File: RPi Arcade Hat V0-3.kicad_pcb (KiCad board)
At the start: 4 copper layers, 241.3 x 64.5 mm, 137 parts, among them J1 Raspberry_Pi_2_3, J10 Coin/Note Input, J11 +24V IN, J12 +12V OUT, J13 Player 1, J14 Player 2, J15 Player 3, J16 Player 4, J17 Counter Board, J18 HDSP-523E, J19 Coin Counter, J2 Player 1, J3 Player 2, J4 Spares, J5 Player 3, J6 Player 4, J7 +24V OUT, J8 Counter Bypass, Q1 BC847, Q10 BC847, Q11 BC847, Q12 BC847, Q13 BC847, Q14 BC847, Q15 BC847, Q16 BC847, Q2 BC847, Q3 BC847, Q4 BC847, Q5 BC847, Q6 BC847, Q7 BC847, Q8 BC847, Q9 BC847, U1 SN74HC32N, U10 NE555DR, U12 SN74HC08N, U13 NE555DR, U14 SN74HC74N, U15 SN74HC32N, U16 SN74HC32N, U18 SN74HC08N, U3 LM2595S-12, U4 4510, U6 4510, U7 4511, U8 4511, U9 NE555DR

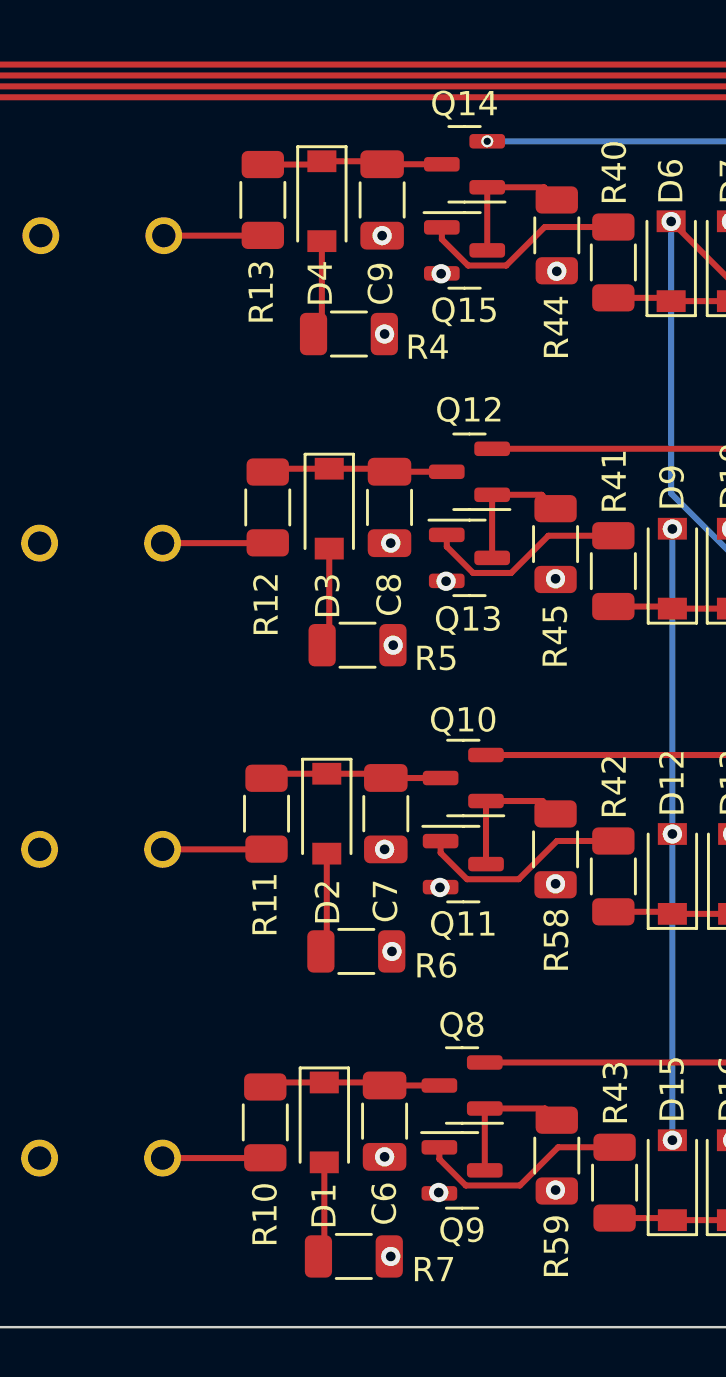
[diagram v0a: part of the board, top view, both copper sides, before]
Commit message: Found Error on Debounce Circuit
As I was going through the schematic I found I wired the button credit input incorrect, and had the logic level held high then pulling to GND, and I should've used an inverter on the output, went with a simple fix, and ended up removing the extra components and changing the connection on the button from GND to +5V
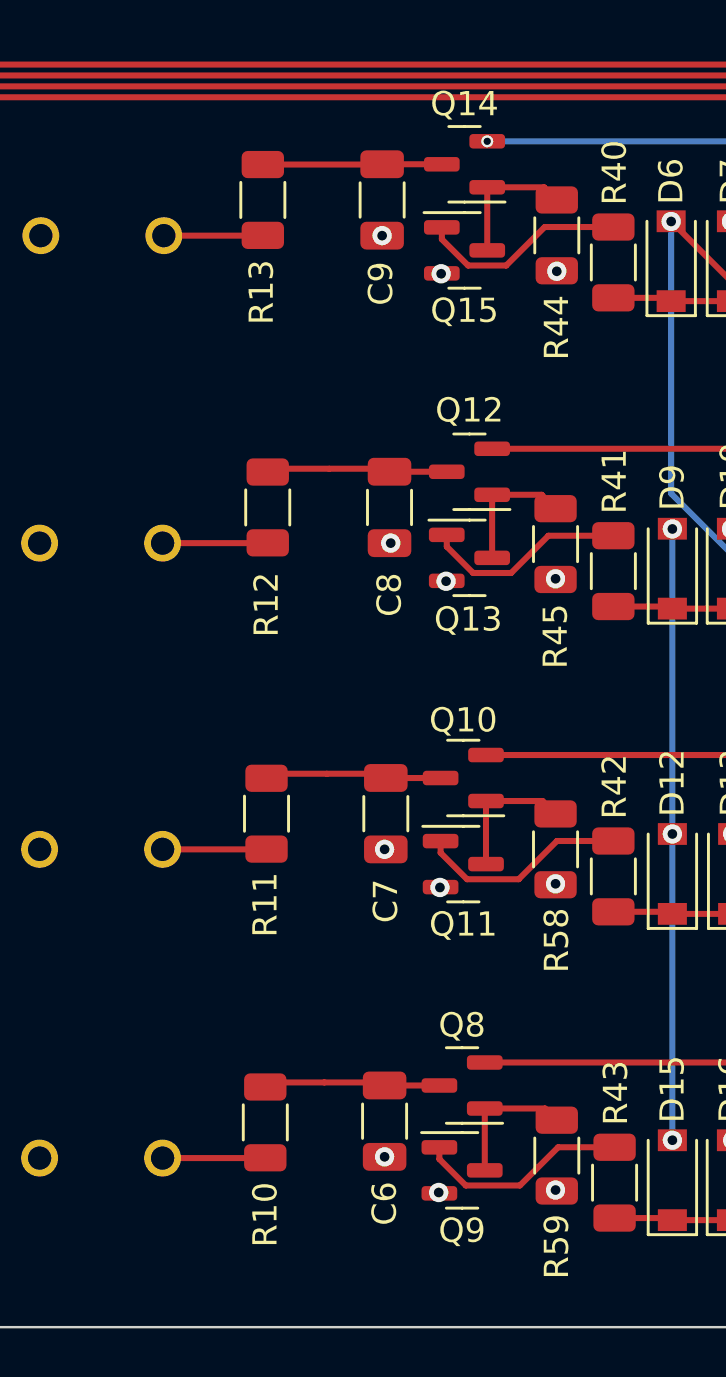
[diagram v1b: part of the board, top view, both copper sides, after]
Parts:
- removed D1, D2, D3, D4: 1N4448W, Diode_SMD:D_SOD-123
- removed R4, R5, R6, R7: 10k, Resistor_SMD:R_1206_3216Metric
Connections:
- J13 pad 1: GND -> +5V
- J14 pad 1: GND -> +5V
- J15 pad 1: GND -> +5V
- J16 pad 1: GND -> +5V
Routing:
- net Net-(D2-Pad2): track 4.14 -> 0.00 mm
- net Net-(D3-Pad2): track 4.11 -> 0.00 mm
- net Net-(D1-Pad2): track 3.99 -> 0.00 mm
- net Net-(D4-Pad2): track 3.98 -> 0.00 mm
- net +5V: vias 25 -> 21

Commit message: Current Changes To Repository
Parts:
- added D1: 1N4448W, Diode_SMD:D_SOD-123, F.Cu at (157.6, 123.6)
- added D2: 1N4448W, Diode_SMD:D_SOD-123, F.Cu at (157.7, 110.9)
- added D3: 1N4448W, Diode_SMD:D_SOD-123, F.Cu at (157.8, 98.3)
- added D4: 1N4448W, Diode_SMD:D_SOD-123, F.Cu at (157.5, 85.6)
- added R4: 10k, Resistor_SMD:R_1206_3216Metric, F.Cu at (158.6, 91.1)
- added R5: 10k, Resistor_SMD:R_1206_3216Metric, F.Cu at (159.0, 103.9)
- added R6: 10k, Resistor_SMD:R_1206_3216Metric, F.Cu at (158.9, 116.6)
- added R7: 10k, Resistor_SMD:R_1206_3216Metric, F.Cu at (158.8, 129.2)
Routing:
- net Net-(D2-Pad2): track 0.00 -> 4.14 mm
- net Net-(D3-Pad2): track 0.00 -> 4.11 mm
- net Net-(D1-Pad2): track 0.00 -> 3.99 mm
- net Net-(D4-Pad2): track 0.00 -> 3.98 mm
- net +5V: vias 21 -> 25
